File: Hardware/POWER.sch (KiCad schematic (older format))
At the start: 22 parts, among them P1 RCA_conn_x2, P3 3.5mm_conn_tip_switch, P4 3.5mm_conn_tip_switch, P43 +5V, Q2 BSS138, SW1 PWR_BTN, U2 LP38692, U3 PLR135/T10, U4 POM-3535L-3-R, U5 POM-3535L-3-R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

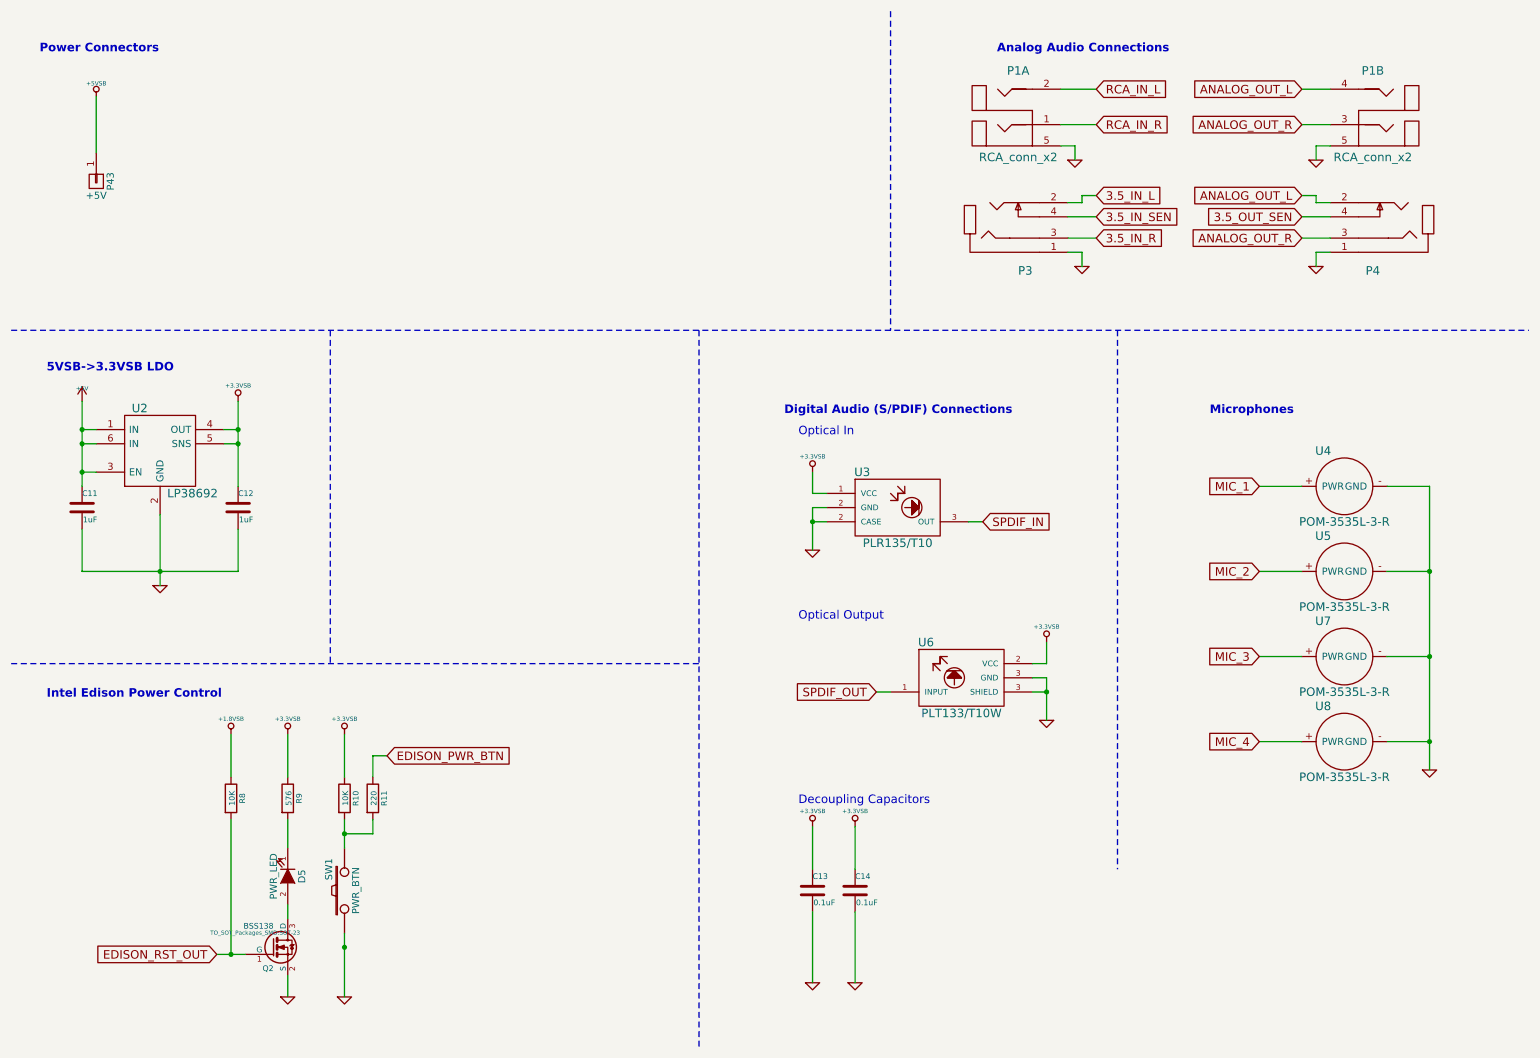
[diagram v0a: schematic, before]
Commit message: All tracks and planes filled.  Fixing fill intersections and missing power/gnd connections
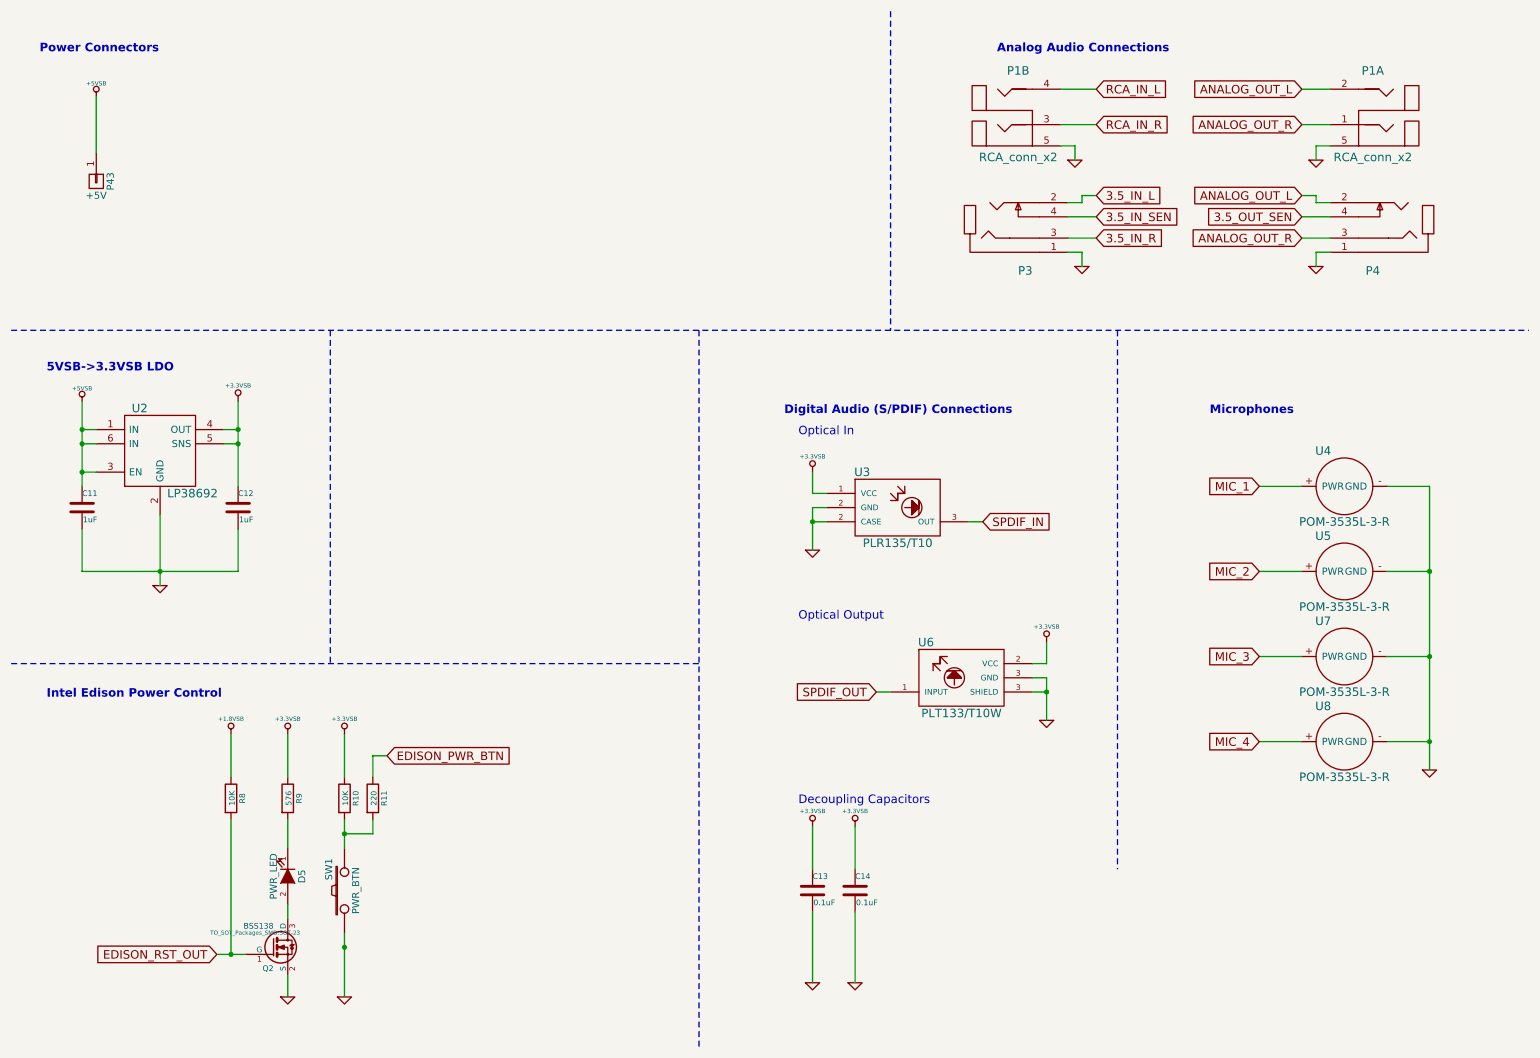
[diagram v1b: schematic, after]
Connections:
- net +5V is gone; now on net +5VSB: C11.1, U2.1 (IN), U2.3 (EN), U2.6 (IN)
- net ANALOG_OUT_L: now also P1.2; no longer P1.4
- net ANALOG_OUT_R: now also P1.1; no longer P1.3
- net RCA_IN_L: now also P1.4; no longer P1.2
- net RCA_IN_R: now also P1.3; no longer P1.1
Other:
- moved on the sheet: P1A, P1B
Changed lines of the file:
@@
 L RCA_conn_x2 P1
 U 1 1 585AC7CF
+P 10100 1300
+F 0 "P1" H 10100 1680 60  0000 C CNN
+F 1 "RCA_conn_x2" H 10100 1070 60  0000 C CNN
+F 2 "muse-v2-lib:PJRAS2X2S01X" H 10110 1300 60  0001 C CNN
+F 3 "" H 10110 1300 60  0000 C CNN
+	1    10100 1300
+	-1   0    0    -1
+$EndComp
+$Comp
+L RCA_conn_x2 P1
+U 2 1 585AC847
 P 7600 1300
 F 0 "P1" H 7600 1680 60  0000 C CNN
@@
 F 2 "muse-v2-lib:PJRAS2X2S01X" H 7610 1300 60  0001 C CNN
 F 3 "" H 7610 1300 60  0000 C CNN
-	1    7600 1300
+	2    7600 1300
 	1    0    0    -1
-$EndComp
-$Comp
-L RCA_conn_x2 P1
-U 2 1 585AC847
-P 10100 1300
-F 0 "P1" H 10100 1680 60  0000 C CNN
-F 1 "RCA_conn_x2" H 10100 1070 60  0000 C CNN
-F 2 "muse-v2-lib:PJRAS2X2S01X" H 10110 1300 60  0001 C CNN
-F 3 "" H 10110 1300 60  0000 C CNN
-	2    10100 1300
-	-1   0    0    -1
 $EndComp
 Wire Wire Line
@@
 Wire Wire Line
 	8000 1450 7900 1450
+Connection ~ 2850 7100
 $Comp
-L +5V #PWR035
-U 1 1 58627E51
+L +5VSB #PWR?
+U 1 1 586E02EE
 P 1000 3250
-F 0 "#PWR035" H 1000 3340 20  0001 C CNN
-F 1 "+5V" H 1000 3340 30  0000 C CNN
+F 0 "#PWR?" H 1000 3340 20  0001 C CNN
+F 1 "+5VSB" H 1000 3340 30  0000 C CNN
 F 2 "" H 1000 3250 60  0000 C CNN
 F 3 "" H 1000 3250 60  0000 C CNN
@@
 	1    0    0    -1
 $EndComp
-Connection ~ 2850 7100
 $EndSCHEMATC
